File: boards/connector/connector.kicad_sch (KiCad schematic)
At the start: 43 parts, among them J1 Conn_01x15, J10 Conn_01x07, J11 Conn_01x07, J12 Conn_01x07, J13 Conn_01x07, J14 CDU_Connector, J15 Conn_02x31_Top_Bottom, J2 Conn_01x15, J3 Conn_01x15, J4 Conn_01x15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

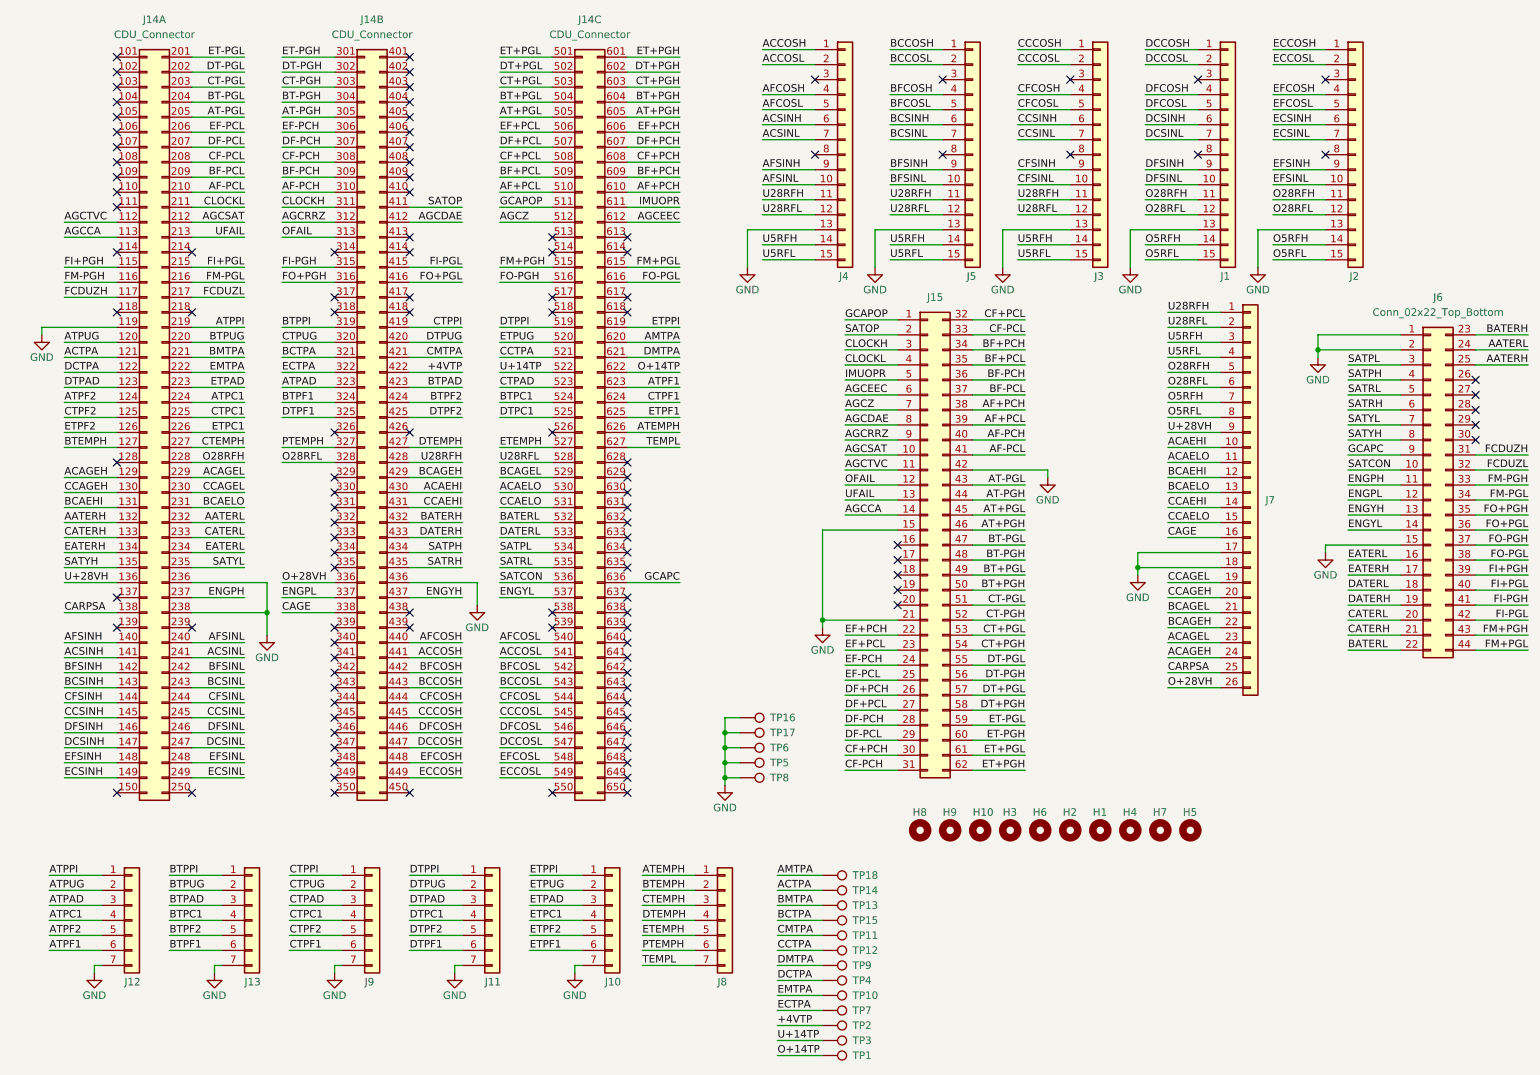
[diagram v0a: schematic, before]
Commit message: Connector board: swap PSA connector for 44-pin, separate resolver and CDU references, and add some more power pins
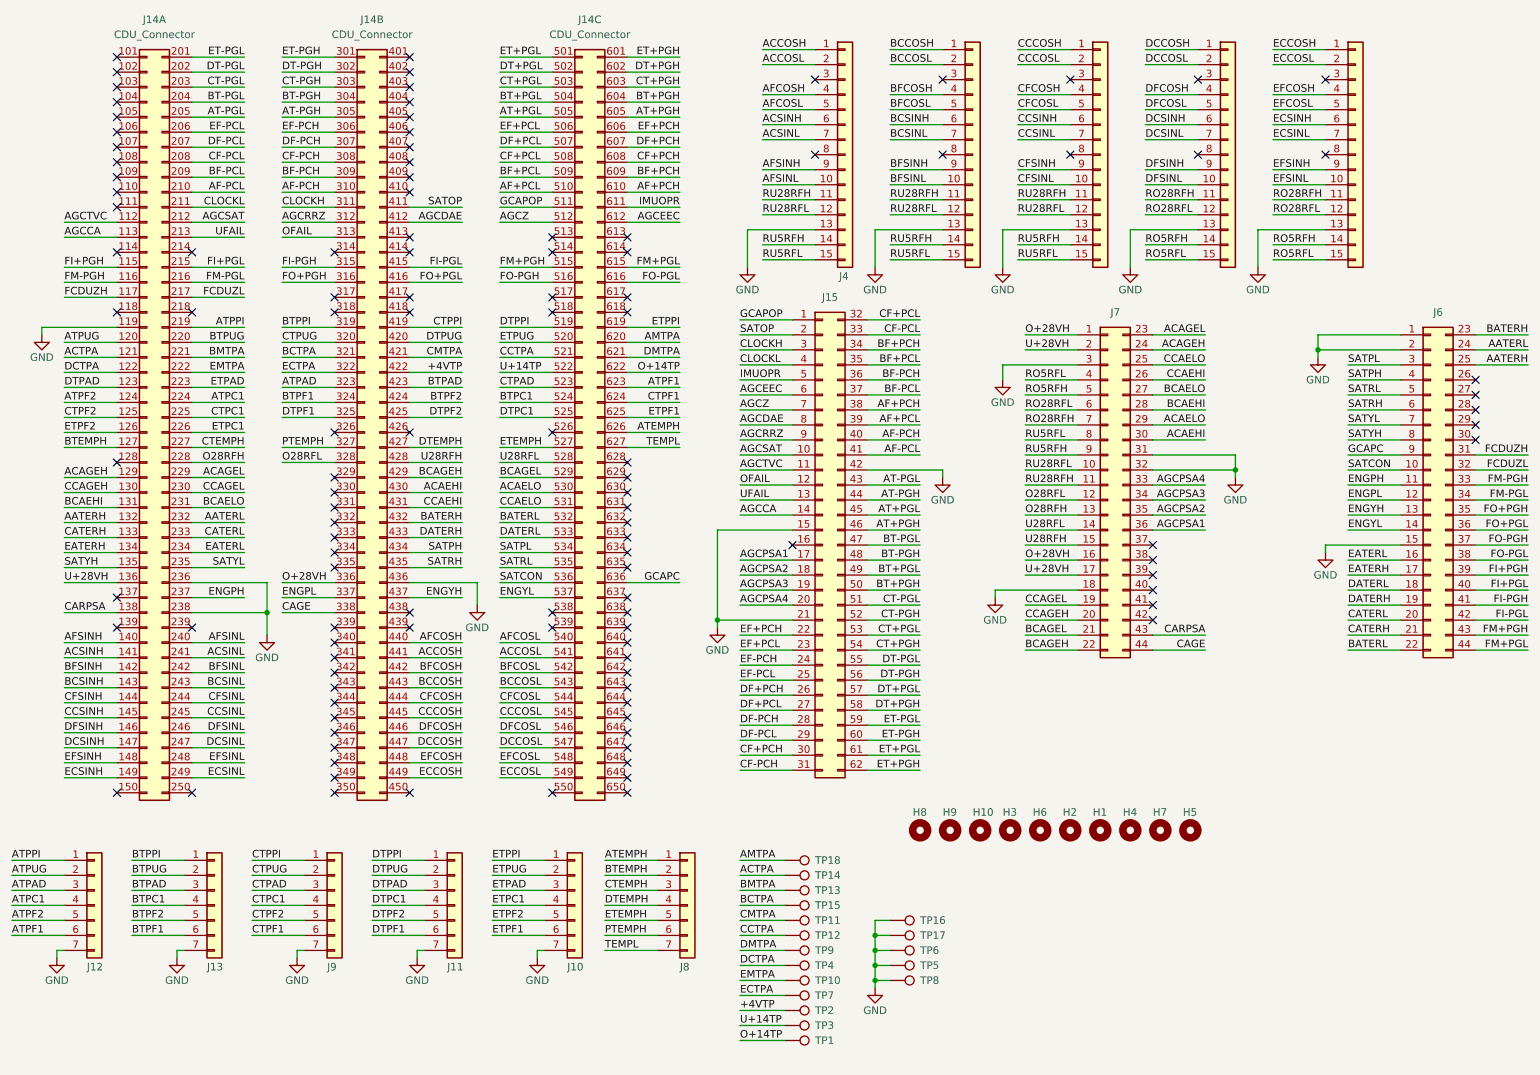
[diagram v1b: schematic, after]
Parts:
- removed J7: Conn_01x26, Connector_Dsub:DSUB-26-HD_Female_Vertical_P2.29x1.98mm_MountingHoles, symbol Connector_Generic:Conn_01x26
- added J7: Conn_02x22_Top_Bottom, Connector_Dsub:DSUB-44-HD_Male_Vertical_P2.29x1.98mm_MountingHoles, symbol Connector_Generic:Conn_02x22_Top_Bottom
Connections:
- net ACAEHI: now also J7.30 (Pin_30)
- net ACAELO: now also J7.29 (Pin_29)
- net ACAGEH: now also J7.24 (Pin_24)
- net ACAGEL: now also J7.23 (Pin_23)
- net BCAEHI: now also J7.28 (Pin_28)
- net BCAELO: now also J7.27 (Pin_27)
- net BCAGEH: now also J7.22 (Pin_22)
- net BCAGEL: now also J7.21 (Pin_21)
- net CAGE: now also J7.44 (Pin_44)
- net CARPSA: now also J7.43 (Pin_43)
- net CCAEHI: now also J7.26 (Pin_26)
- net CCAELO: now also J7.25 (Pin_25)
- net CCAGEH: now also J7.20 (Pin_20)
- net CCAGEL: now also J7.19 (Pin_19)
- net GND: now also J7.18 (Pin_18), J7.3 (Pin_3), J7.31 (Pin_31), J7.32 (Pin_32)
- net O+28VH: now also J7.1 (Pin_1), J7.16 (Pin_16)
- net O28RFH: now also J7.13 (Pin_13); no longer J1.11 (Pin_11), J2.11 (Pin_11)
- net O28RFL: now also J7.12 (Pin_12); no longer J1.12 (Pin_12), J2.12 (Pin_12)
- net U+28VH: now also J7.17 (Pin_17), J7.2 (Pin_2)
- net U28RFH: now also J7.15 (Pin_15); no longer J3.11 (Pin_11), J4.11 (Pin_11), J5.11 (Pin_11)
- net U28RFL: now also J7.14 (Pin_14); no longer J3.12 (Pin_12), J4.12 (Pin_12), J5.12 (Pin_12)
- net AGCPSA1: now reaches J15.17 (Pin_17)
- net AGCPSA1: now also J7.36 (Pin_36)
- net AGCPSA2: now reaches J15.18 (Pin_18)
- net AGCPSA2: now also J7.35 (Pin_35)
- net AGCPSA3: now reaches J15.19 (Pin_19)
- net AGCPSA3: now also J7.34 (Pin_34)
- net AGCPSA4: now reaches J15.20 (Pin_20)
- net AGCPSA4: now also J7.33 (Pin_33)
- net O5RFH renamed RO5RFH
- net RO5RFH: now also J7.5 (Pin_5)
- net O5RFL renamed RO5RFL
- net RO5RFL: now also J7.4 (Pin_4)
- net U5RFH renamed RU5RFH
- net RU5RFH: now also J7.9 (Pin_9)
- net U5RFL renamed RU5RFL
- net RU5RFL: now also J7.8 (Pin_8)
- new net RO28RFH: J1.11 (Pin_11), J2.11 (Pin_11), J7.7 (Pin_7)
- new net RO28RFL: J1.12 (Pin_12), J2.12 (Pin_12), J7.6 (Pin_6)
- new net RU28RFH: J3.11 (Pin_11), J4.11 (Pin_11), J5.11 (Pin_11), J7.11 (Pin_11)
- new net RU28RFL: J3.12 (Pin_12), J4.12 (Pin_12), J5.12 (Pin_12), J7.10 (Pin_10)
- no-connect marks 116 -> 118
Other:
- moved on the sheet: J10, J11, J12, J13, J15, J8, J9, TP1, TP10, TP11, TP12, TP13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
